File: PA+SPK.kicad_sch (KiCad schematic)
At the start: 25 parts, among them J2 4 Ohm SPEAKER, J4 PJ-342 / PJ-393-A, Q2 AO3400A, U10 74LVC1G08, U2 NS4150

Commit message: Initial population of PCB
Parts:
- U10: footprint (none) -> Package_TO_SOT_SMD:SOT-23-5
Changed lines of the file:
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@@
 			)
 		)
-		(property "Footprint" ""
+		(property "Footprint" "Package_TO_SOT_SMD:SOT-23-5"
 			(at 234.95 41.91 0)
 			(effects

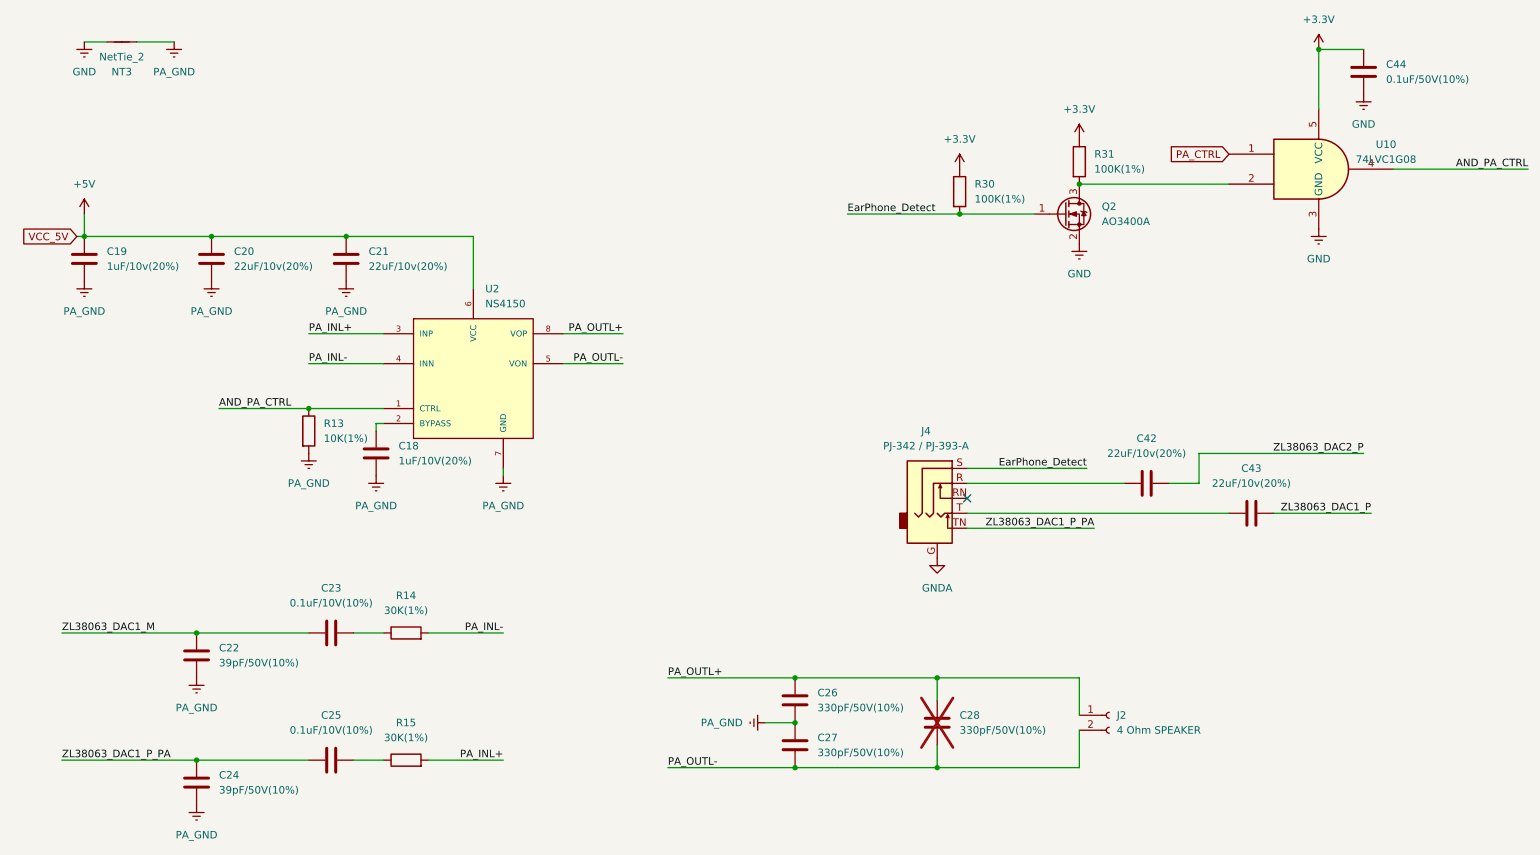
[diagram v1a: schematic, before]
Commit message: Added DSP, Neopixles, MIC's and mounting holes
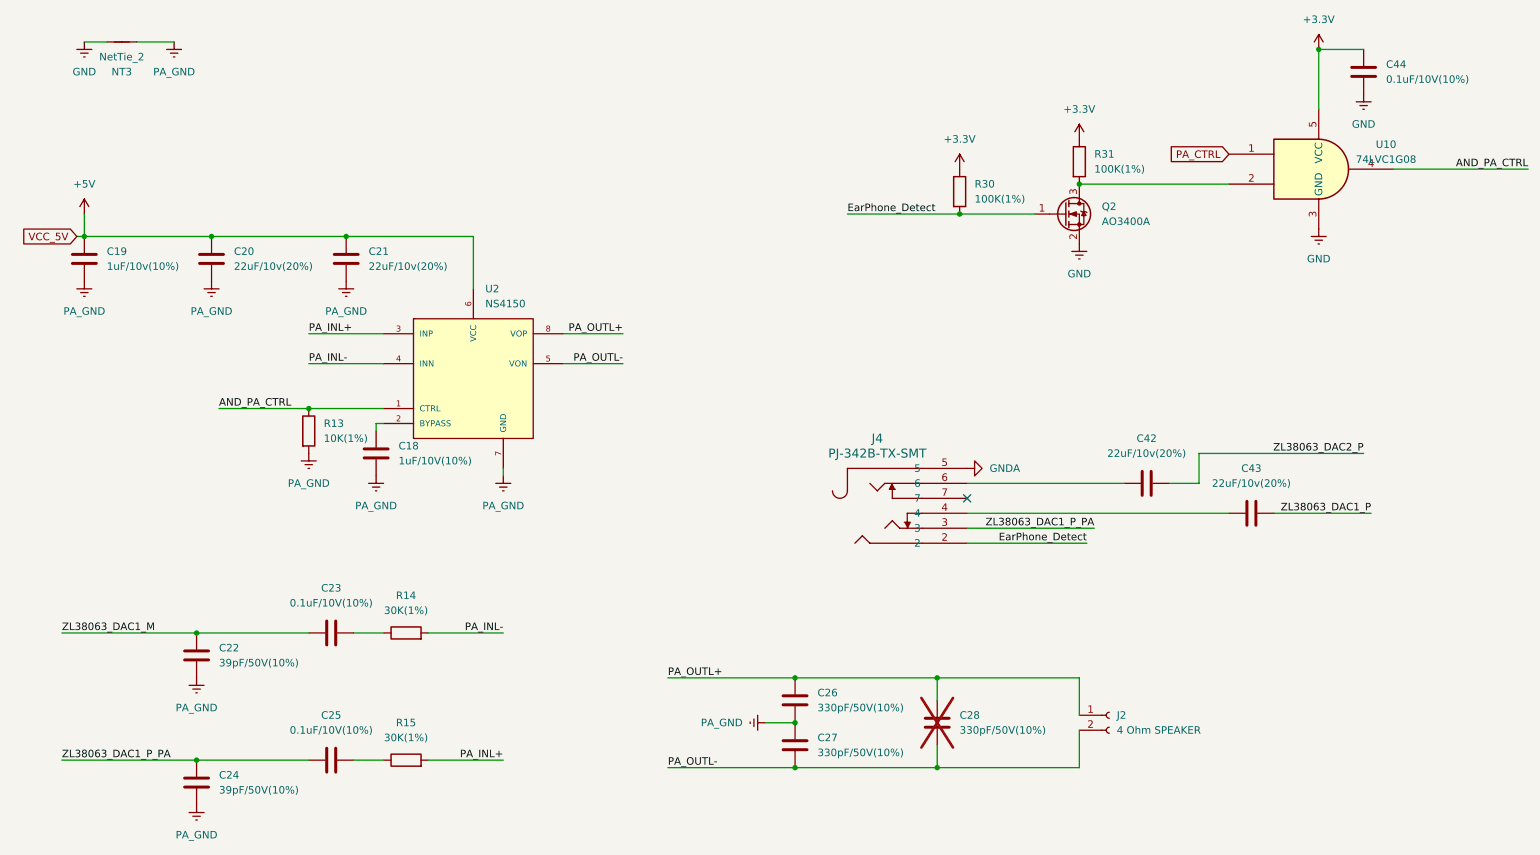
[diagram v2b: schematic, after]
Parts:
- removed J4: PJ-342 / PJ-393-A, Connector_Audio:Jack_3.5mm_PJ311_Horizontal, symbol Connector_Audio:AudioJack3_Ground_SwitchTR
- added J4: PJ-342B-TX-SMT, PJ-342B-TX-SMT_XKB, symbol PJ-342B:PJ-342B-TX-SMT
- C18: value 1uF/10V(20%) -> 1uF/10V(10%); footprint Capacitor_SMD:C_0603_1608Metric -> Capacitor_SMD:C_0402_1005Metric
- C19: value 1uF/10v(20%) -> 1uF/10v(10%); footprint Capacitor_SMD:C_0603_1608Metric -> Capacitor_SMD:C_0402_1005Metric
- C20, C21, C22, C23, C24, C25, C26, C27, C28, C42, C43: footprint Capacitor_SMD:C_0603_1608Metric -> Capacitor_SMD:C_0402_1005Metric
- C44: value 0.1uF/50V(10%) -> 0.1uF/10V(10%); footprint Capacitor_SMD:C_0603_1608Metric -> Capacitor_SMD:C_0402_1005Metric
- R13, R14, R15, R30, R31: footprint Resistor_SMD:R_0603_1608Metric -> Resistor_SMD:R_0402_1005Metric
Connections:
- net EarPhone_Detect: now also J4.2
- net GNDA: now also J4.5
- net ZL38063_DAC1_P_PA: now also J4.3
- net at C43.1: now also J4.4
- net at C42.1: now also J4.6
